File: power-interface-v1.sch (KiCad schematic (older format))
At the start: 10 parts, among them P1 PINBALL-CONNECTOR, P10 CONN_01X01, P2 PINBALL-CONNECTOR, P3 PINBALL-CONNECTOR, P4 PINBALL-CONNECTOR, P5 CONN_01X01, P6 CONN_01X01, P7 CONN_01X01, P8 CONN_01X01, P9 CONN_01X01

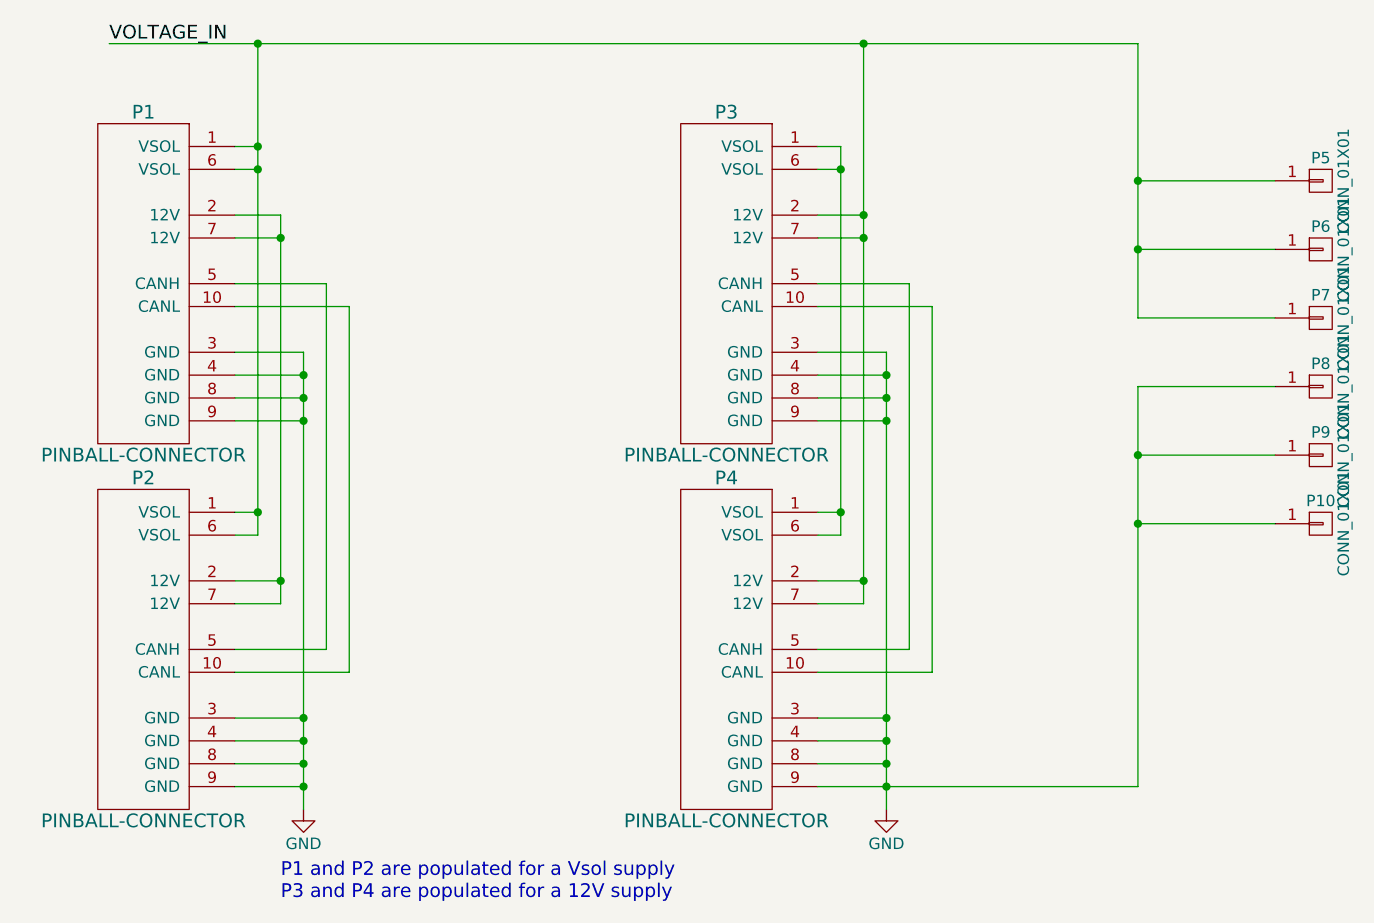
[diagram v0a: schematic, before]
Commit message: Updating power interface to use fuses, and to use them to choose between a 12V and Vsol supply
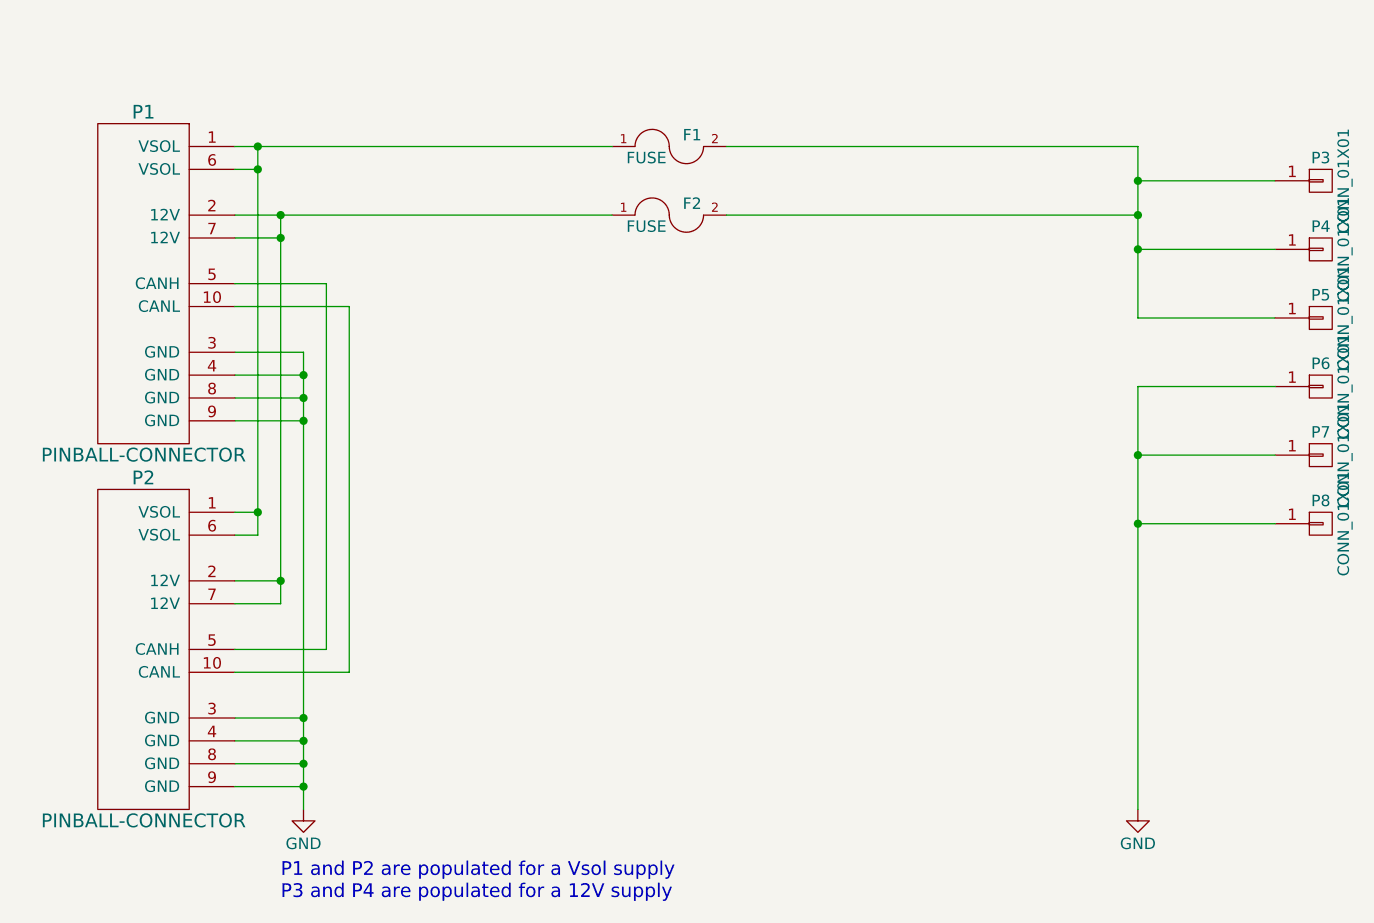
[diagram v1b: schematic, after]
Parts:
- removed P3, P4: PINBALL-CONNECTOR, Pinball:PINBALL-CONNECTOR-V, symbol PINBALL-CONNECTOR
- added F1, F2: FUSE, Pinball:FC203-20MM, symbol FUSE
- renumbered P5 to P3, P6 to P4, P7 to P5, P8 to P6, P9 to P7, P10 to P8
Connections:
- net at P1.2 (12V), P1.7 (12V), P2.2 (12V)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: now also F2.1
- net VOLTAGE_IN: no longer names the net of P1.1 (VSOL), P1.6 (VSOL), P2.1 (VSOL), P2.6 (VSOL)
- net VOLTAGE_IN: now also F1.1; no longer P3.1 (P1), P4.1 (P1), P5.1 (P1)
- new net: F1.2, F2.2, P3.1 (P1), P4.1 (P1), P5.1 (P1)
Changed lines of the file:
@@
 LIBS:valves
 LIBS:diypinball-parts
+LIBS:power-interface-v1-cache
 EELAYER 25 0
 EELAYER END
@@
 $EndComp
 $Comp
-L GND #PWR1
+L GND #PWR01
 U 1 1 561D6789
 P 4750 6050
-F 0 "#PWR1" H 4750 5800 50  0001 C CNN
+F 0 "#PWR01" H 4750 5800 50  0001 C CNN
 F 1 "GND" H 4750 5900 50  0000 C CNN
 F 2 "" H 4750 6050 60  0000 C CNN
@@
 	1    0    0    -1
 $EndComp
-Wire Wire Line
-	4550 4750 4450 4750
-Wire Wire Line
-	4550 3150 4450 3150
-Connection ~ 4550 4750
-Wire Wire Line
-	4550 3250 4450 3250
-Connection ~ 4550 3250
-Wire Wire Line
-	4450 3450 4650 3450
-Wire Wire Line
-	4650 5050 4450 5050
-Connection ~ 4650 5050
-Wire Wire Line
-	4650 3550 4450 3550
-Connection ~ 4650 3550
-Wire Wire Line
-	4450 4050 4750 4050
-Wire Wire Line
-	4750 5950 4450 5950
-Connection ~ 4750 5950
-Wire Wire Line
-	4750 5850 4450 5850
-Connection ~ 4750 5850
-Wire Wire Line
-	4750 5750 4450 5750
-Connection ~ 4750 5750
-Wire Wire Line
-	4750 5650 4450 5650
-Connection ~ 4750 5650
-Wire Wire Line
-	4750 4350 4450 4350
-Connection ~ 4750 4350
-Wire Wire Line
-	4750 4250 4450 4250
-Connection ~ 4750 4250
-Wire Wire Line
-	4450 4150 4750 4150
-Connection ~ 4750 4150
-Wire Wire Line
-	4450 3750 4850 3750
-Wire Wire Line
-	4450 3850 4950 3850
-Wire Wire Line
-	4750 4050 4750 6050
-Wire Wire Line
-	4450 5450 4950 5450
-Wire Wire Line
-	4950 5450 4950 3850
-Wire Wire Line
-	4450 5350 4850 5350
-Wire Wire Line
-	4850 5350 4850 3750
-Wire Wire Line
-	4550 2700 4550 4850
-Wire Wire Line
-	4550 4850 4450 4850
-Wire Wire Line
-	4650 3450 4650 5150
-Wire Wire Line
-	4650 5150 4450 5150
-$Comp
-L PINBALL-CONNECTOR P3
-U 1 1 561F2B01
-P 6600 3750
-F 0 "P3" H 6600 4500 60  0000 C CNN
-F 1 "PINBALL-CONNECTOR" H 6600 3000 60  0000 C CNN
-F 2 "Pinball:PINBALL-CONNECTOR-V" H 6800 3800 60  0001 C CNN
-F 3 "" H 6800 3800 60  0000 C CNN
-	1    6600 3750
-	1    0    0    -1
-$EndComp
-$Comp
-L PINBALL-CONNECTOR P4
-U 1 1 561F2B07
-P 6600 5350
-F 0 "P4" H 6600 6100 60  0000 C CNN
-F 1 "PINBALL-CONNECTOR" H 6600 4600 60  0000 C CNN
-F 2 "Pinball:PINBALL-CONNECTOR-V" H 6800 5400 60  0001 C CNN
-F 3 "" H 6800 5400 60  0000 C CNN
-	1    6600 5350
-	1    0    0    -1
-$EndComp
-$Comp
-L GND #PWR2
-U 1 1 561F2B0D
-P 7300 6050
-F 0 "#PWR2" H 7300 5800 50  0001 C CNN
-F 1 "GND" H 7300 5900 50  0000 C CNN
-F 2 "" H 7300 6050 60  0000 C CNN
-F 3 "" H 7300 6050 60  0000 C CNN
-	1    7300 6050
-	1    0    0    -1
-$EndComp
-Wire Wire Line
-	7100 4750 7000 4750
-Wire Wire Line
-	7100 3150 7000 3150
-Connection ~ 7100 4750
-Wire Wire Line
-	7100 3250 7000 3250
-Connection ~ 7100 3250
-Wire Wire Line
-	7000 3450 7200 3450
-Wire Wire Line
-	7200 5050 7000 5050
-Connection ~ 7200 5050
-Wire Wire Line
-	7200 3550 7000 3550
-Connection ~ 7200 3550
-Wire Wire Line
-	7000 4050 7300 4050
-Wire Wire Line
-	7000 5950 8400 5950
-Connection ~ 7300 5950
-Wire Wire Line
-	7300 5850 7000 5850
-Connection ~ 7300 5850
-Wire Wire Line
-	7300 5750 7000 5750
-Connection ~ 7300 5750
-Wire Wire Line
-	7300 5650 7000 5650
-Connection ~ 7300 5650
-Wire Wire Line
-	7300 4350 7000 4350
-Connection ~ 7300 4350
-Wire Wire Line
-	7300 4250 7000 4250
-Connection ~ 7300 4250
-Wire Wire Line
-	7000 4150 7300 4150
-Connection ~ 7300 4150
-Wire Wire Line
-	7000 3750 7400 3750
-Wire Wire Line
-	7000 3850 7500 3850
-Wire Wire Line
-	7300 4050 7300 6050
-Wire Wire Line
-	7000 5450 7500 5450
-Wire Wire Line
-	7500 5450 7500 3850
-Wire Wire Line
-	7000 5350 7400 5350
-Wire Wire Line
-	7400 5350 7400 3750
-Wire Wire Line
-	7100 3150 7100 4850
-Wire Wire Line
-	7100 4850 7000 4850
-Wire Wire Line
-	7200 2700 7200 5150
-Wire Wire Line
-	7200 5150 7000 5150
 Text Notes 4650 6450 0    60   ~ 0
 P1 and P2 are populated for a Vsol supply\nP3 and P4 are populated for a 12V supply
-Text Label 3900 2700 0    60   ~ 0
-VOLTAGE_IN
-Wire Wire Line
-	3900 2700 8400 2700
-Connection ~ 7200 3450
-Connection ~ 4550 2700
-Connection ~ 4550 3150
-$Comp
-L CONN_01X01 P5
+$Comp
+L CONN_01X01 P3
 U 1 1 561F2E9C
 P 9200 3300
-F 0 "P5" H 9200 3400 50  0000 C CNN
+F 0 "P3" H 9200 3400 50  0000 C CNN
 F 1 "CONN_01X01" V 9300 3300 50  0000 C CNN
 F 2 "Pinball:PSU-HOLE" H 9200 3300 60  0001 C CNN
@@
 $EndComp
 $Comp
-L CONN_01X01 P6
+L CONN_01X01 P4
 U 1 1 561F2F29
 P 9200 3600
-F 0 "P6" H 9200 3700 50  0000 C CNN
+F 0 "P4" H 9200 3700 50  0000 C CNN
 F 1 "CONN_01X01" V 9300 3600 50  0000 C CNN
 F 2 "Pinball:PSU-HOLE" H 9200 3600 60  0001 C CNN
@@
 $EndComp
 $Comp
-L CONN_01X01 P7
+L CONN_01X01 P5
 U 1 1 561F2F62
 P 9200 3900
-F 0 "P7" H 9200 4000 50  0000 C CNN
+F 0 "P5" H 9200 4000 50  0000 C CNN
 F 1 "CONN_01X01" V 9300 3900 50  0000 C CNN
 F 2 "Pinball:PSU-HOLE" H 9200 3900 60  0001 C CNN
@@
 $EndComp
 $Comp
-L CONN_01X01 P8
+L CONN_01X01 P6
 U 1 1 561F2F85
 P 9200 4200
-F 0 "P8" H 9200 4300 50  0000 C CNN
+F 0 "P6" H 9200 4300 50  0000 C CNN
 F 1 "CONN_01X01" V 9300 4200 50  0000 C CNN
 F 2 "Pinball:PSU-HOLE" H 9200 4200 60  0001 C CNN
@@
 $EndComp
 $Comp
-L CONN_01X01 P9
+L CONN_01X01 P7
 U 1 1 561F2FAA
 P 9200 4500
-F 0 "P9" H 9200 4600 50  0000 C CNN
+F 0 "P7" H 9200 4600 50  0000 C CNN
 F 1 "CONN_01X01" V 9300 4500 50  0000 C CNN
 F 2 "Pinball:PSU-HOLE" H 9200 4500 60  0001 C CNN
@@
 $EndComp
 $Comp
-L CONN_01X01 P10
+L CONN_01X01 P8
 U 1 1 561F2FD1
 P 9200 4800
-F 0 "P10" H 9200 4900 50  0000 C CNN
+F 0 "P8" H 9200 4900 50  0000 C CNN
 F 1 "CONN_01X01" V 9300 4800 50  0000 C CNN
 F 2 "Pinball:PSU-HOLE" H 9200 4800 60  0001 C CNN
@@
 	1    0    0    -1
 $EndComp
-Wire Wire Line
-	9000 3900 8400 3900
-Wire Wire Line
-	8400 3900 8400 2700
-Connection ~ 7200 2700
+$Comp
+L GND #PWR02
+U 1 1 5620DE7E
+P 8400 6050
+F 0 "#PWR02" H 8400 5800 50  0001 C CNN
+F 1 "GND" H 8400 5900 50  0000 C CNN
+F 2 "" H 8400 6050 60  0000 C CNN
+F 3 "" H 8400 6050 60  0000 C CNN
+	1    8400 6050
+	1    0    0    -1
+$EndComp
+Wire Wire Line
+	4550 4750 4450 4750
+Connection ~ 4550 4750
+Wire Wire Line
+	4550 3250 4450 3250
+Connection ~ 4550 3250
+Wire Wire Line
+	4450 3450 6100 3450
+Wire Wire Line
+	4650 5050 4450 5050
+Connection ~ 4650 5050
+Wire Wire Line
+	4650 3550 4450 3550
+Connection ~ 4650 3550
+Wire Wire Line
+	4450 4050 4750 4050
+Wire Wire Line
+	4750 5950 4450 5950
+Connection ~ 4750 5950
+Wire Wire Line
+	4750 5850 4450 5850
+Connection ~ 4750 5850
+Wire Wire Line
+	4750 5750 4450 5750
+Connection ~ 4750 5750
+Wire Wire Line
+	4750 5650 4450 5650
+Connection ~ 4750 5650
+Wire Wire Line
+	4750 4350 4450 4350
+Connection ~ 4750 4350
+Wire Wire Line
+	4750 4250 4450 4250
+Connection ~ 4750 4250
+Wire Wire Line
+	4450 4150 4750 4150
+Connection ~ 4750 4150
+Wire Wire Line
+	4450 3750 4850 3750
+Wire Wire Line
+	4450 3850 4950 3850
+Wire Wire Line
+	4750 4050 4750 6050
+Wire Wire Line
+	4450 5450 4950 5450
+Wire Wire Line
+	4950 5450 4950 3850
+Wire Wire Line
+	4450 5350 4850 5350
+Wire Wire Line
+	4850 5350 4850 3750
+Wire Wire Line
+	4550 3150 4550 4850
+Wire Wire Line
+	4550 4850 4450 4850
+Wire Wire Line
+	4650 3450 4650 5150
+Wire Wire Line
+	4650 5150 4450 5150
+Wire Wire Line
+	8400 3900 9000 3900
 Wire Wire Line
 	9000 3600 8400 3600
@@
 	9000 4200 8400 4200
 Wire Wire Line
-	8400 4200 8400 5950
+	8400 4200 8400 6050
 Wire Wire Line
 	9000 4500 8400 4500
@@
 	9000 4800 8400 4800
 Connection ~ 8400 4800
+Wire Wire Line
+	8400 3150 8400 3900
+Wire Wire Line
+	4450 3150 6100 3150
+$Comp
+L FUSE F1
+U 1 1 5620E088
+P 6350 3150
+F 0 "F1" H 6450 3200 50  0000 C CNN
+F 1 "FUSE" H 6250 3100 50  0000 C CNN
+F 2 "Pinball:FC203-20MM" H 6350 3150 60  0001 C CNN
+F 3 "" H 6350 3150 60  0000 C CNN
+	1    6350 3150
+	1    0    0    -1
+$EndComp
+$Comp
+L FUSE F2
+U 1 1 5620E11F
+P 6350 3450
+F 0 "F2" H 6450 3500 50  0000 C CNN
+F 1 "FUSE" H 6250 3400 50  0000 C CNN
+F 2 "Pinball:FC203-20MM" H 6350 3450 60  0001 C CNN
+F 3 "" H 6350 3450 60  0000 C CNN
+	1    6350 3450
+	1    0    0    -1
+$EndComp
+Connection ~ 4650 3450
+Connection ~ 4550 3150
+Wire Wire Line
+	6600 3150 8400 3150
+Wire Wire Line
+	6600 3450 8400 3450
+Connection ~ 8400 3450
 $EndSCHEMATC
